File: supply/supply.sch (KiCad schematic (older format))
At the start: 35 parts

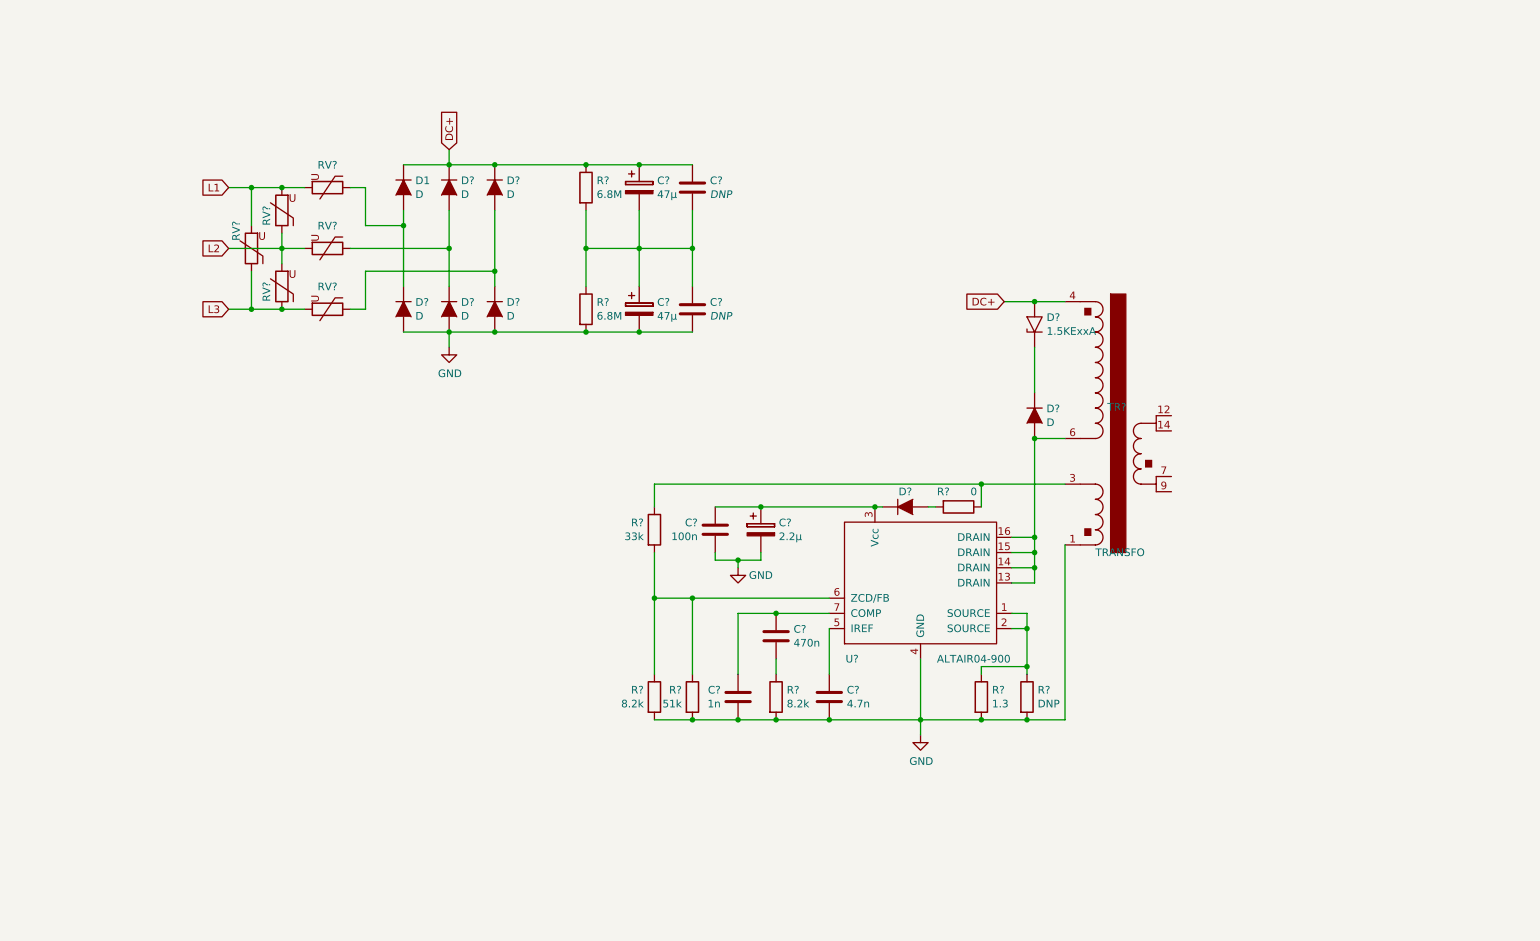
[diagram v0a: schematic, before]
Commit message: Add Li charger/protection
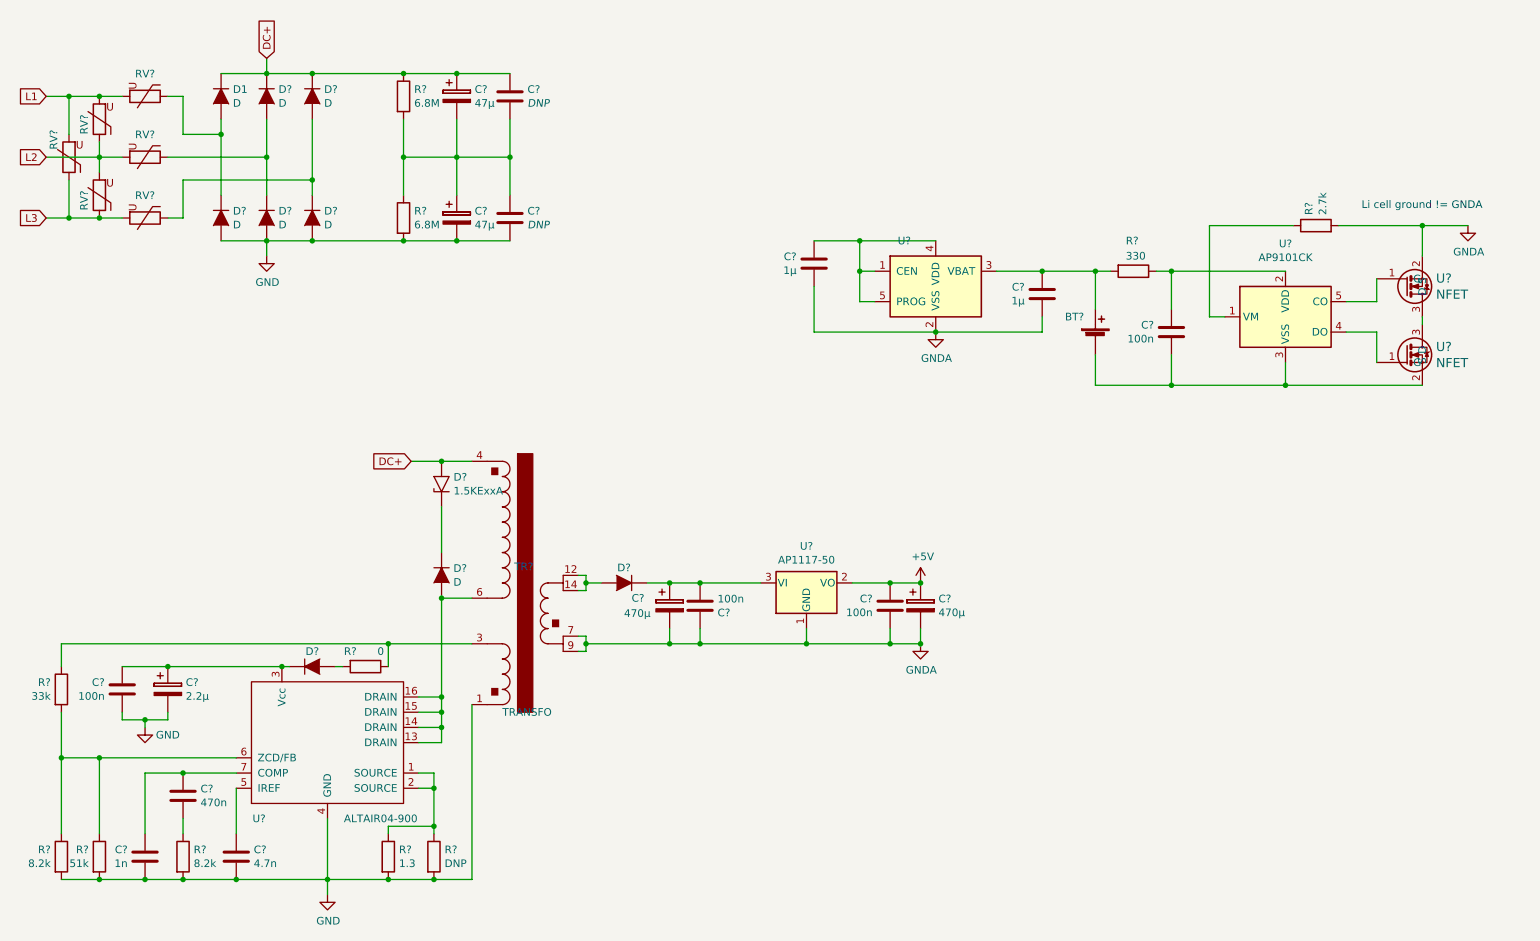
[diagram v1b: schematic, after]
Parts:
- added BT?: Battery_Cell, symbol Device:Battery_Cell
- added C? (x2): 470µ, symbol stmbl:CP
- added C? (x3): 100n, stmbl:C_0805, symbol stmbl:C
- added C? (x2): 1µ, stmbl:C_0805, symbol stmbl:C
- added D?: D, stmbl:SMA_Standard, symbol stmbl:D
- added R?: 330, stmbl:R_0805, symbol stmbl:R
- added R?: 2.7k, stmbl:R_0805, symbol stmbl:R
- added U?: AP1117-50, Package_TO_SOT_SMD:SOT-223-3_TabPin2, symbol Regulator_Linear:AP1117-50
- added U?: MCP73811T-420I-OT, Package_TO_SOT_SMD:SOT-23-5, symbol Battery_Management:MCP73811T-420I-OT
- added U?: AP9101CK, Package_TO_SOT_SMD:SOT-23-5, symbol Battery_Management:AP9101CK
- added U? (x2): NFET, symbol stmbl:NFET
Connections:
- net at TR?.12: now also TR?.14, D?.2 (A)
- net GNDA: now reaches TR?.7
- net GNDA: now also TR?.9, C?.1, C?.2, C?.2, C?.2, C?.2, C?.2, R?.2, U?.1 (GND), U?.2 (S), U?.2 (VSS)
- new net: C?.1, C?.2, D?.1 (K), U?.3 (VI)
- new net: C?.1, U?.1 (CEN), U?.4 (VDD), U?.5 (PROG)
- new net: BT?.1 (+), C?.1, R?.2, U?.3 (VBAT)
- new net: R?.1, U?.1 (VM)
- new net: C?.1, R?.1, U?.2 (VDD)
- new net: BT?.2 (-), C?.2, U?.2 (S), U?.3 (VSS)
- new net: U?.1 (G), U?.4 (DO)
- new net: U?.1 (G), U?.5 (CO)
- new net: U?.3 (D), U?.3 (D)
- new net +5V: C?.1, C?.1, U?.2 (VO)
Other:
- note added: "Li cell ground != GNDA"
- moved on the sheet: C?, D1, D?, R?, RV?, TR?, U?
